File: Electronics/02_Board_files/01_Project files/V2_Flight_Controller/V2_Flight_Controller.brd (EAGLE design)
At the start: 160 x 100 mm, 73 parts

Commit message: 1. Added bmp180.lbr, made changes in 1.25pitch programming connector library 2. Added Datasheets/05_Motor_control/SI2302.pdf 3. Completed top placement for v2 pcb layout
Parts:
- removed 01_BATTERY_PROTECTION_AND_MONITORING:TP_5V: TPB1,27, testpad:B1,27
- added 05_SENSOR:C1, 05_SENSOR:C2: 2.2nF, 50V, ±10%, adafruit:C0603
- added 05_SENSOR:U1: BMP180, bmp180:BMP180
- 07_CONNECTORS:X706: device con-molex:53047-05 -> con-molex_modified:53047-05
- moved 05_SENSOR:C503 276.3 mm to (64.4, 16.0), flipped to the bottom
- moved 05_SENSOR:C502 267.9 mm to (64.2, 12.0), flipped to the bottom
- moved 05_SENSOR:C501 262.5 mm to (66.0, 7.02), flipped to the bottom
- moved 05_SENSOR:R502 258.4 mm to (74.7, 6.02), flipped to the bottom
- moved 06_MOTOR_CONTROL:R604 246.9 mm to (13.0, 3.38), turned to 180 degrees
- moved 06_MOTOR_CONTROL:R603 238.5 mm to (27.0, 5.62)
- moved 06_MOTOR_CONTROL:D603 236.4 mm to (35.5, 8.00)
- moved 05_SENSOR:C504 236.0 mm to (72.6, 20.2), flipped to the bottom
- moved 05_SENSOR:U501 236.0 mm to (72.6, 12.6), flipped to the bottom
- moved 05_SENSOR:R501 233.4 mm to (65.5, 19.0), flipped to the bottom
- moved 06_MOTOR_CONTROL:D604 233.0 mm to (35.5, 32.0), turned to 180 degrees
- moved 06_MOTOR_CONTROL:Q603 232.9 mm to (31.2, 4.50), turned to 270 degrees
- moved 06_MOTOR_CONTROL:R606 232.2 mm to (27.0, 3.38)
- moved 06_MOTOR_CONTROL:R608 230.8 mm to (27.0, 36.6)
- moved 06_MOTOR_CONTROL:Q604 223.7 mm to (31.2, 35.5), turned to 270 degrees
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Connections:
- net +3V3: now also 05_SENSOR:C1.1, 05_SENSOR:C2.1, 05_SENSOR:U1.2, 05_SENSOR:U1.3
- net +5V: no longer 01_BATTERY_PROTECTION_AND_MONITORING:TP_5V.TP
- net 05_SENSOR:SCL: now also 05_SENSOR:U1.5
- net 05_SENSOR:SDA: now also 05_SENSOR:U1.6
- net GND: now also 05_SENSOR:C1.2, 05_SENSOR:C2.2, 05_SENSOR:U1.7
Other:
- board size 160 x 100 mm -> 40 x 40 mm

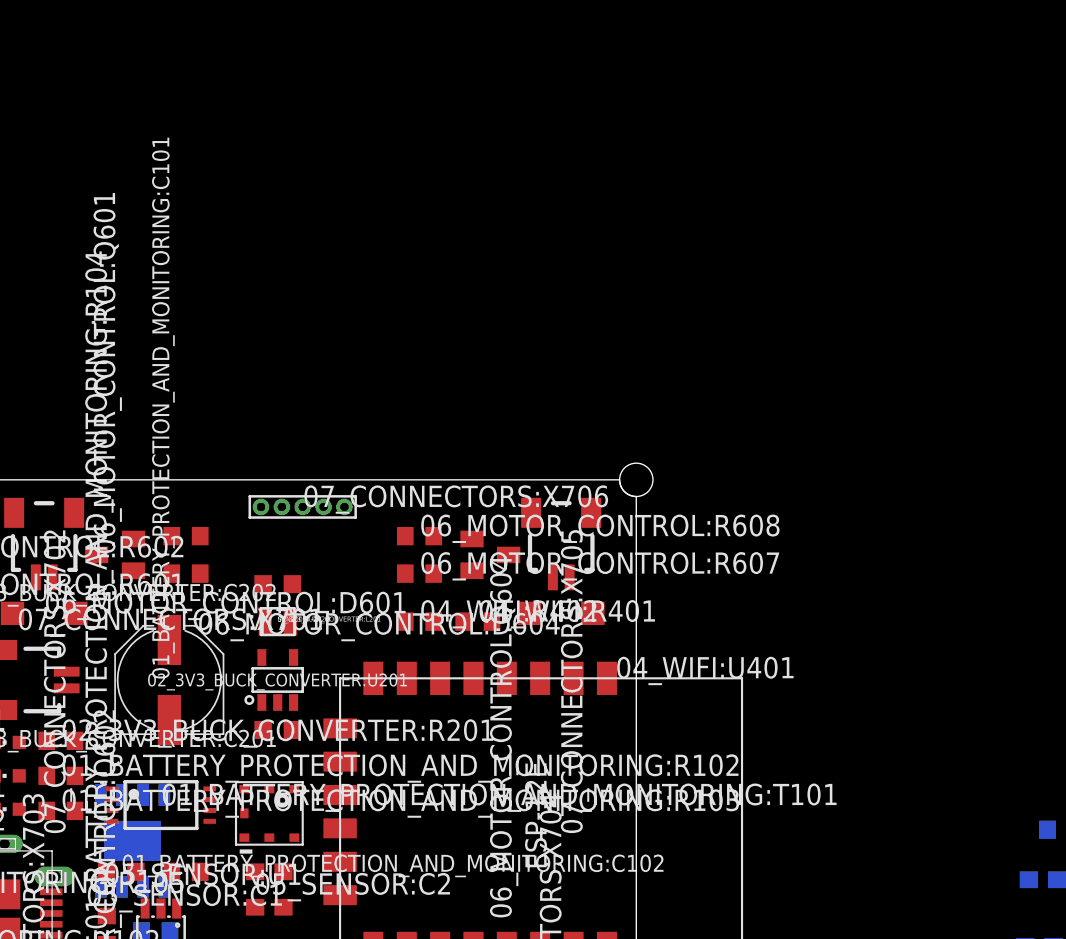
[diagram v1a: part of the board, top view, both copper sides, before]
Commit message: 1. added a bigger input capacitor
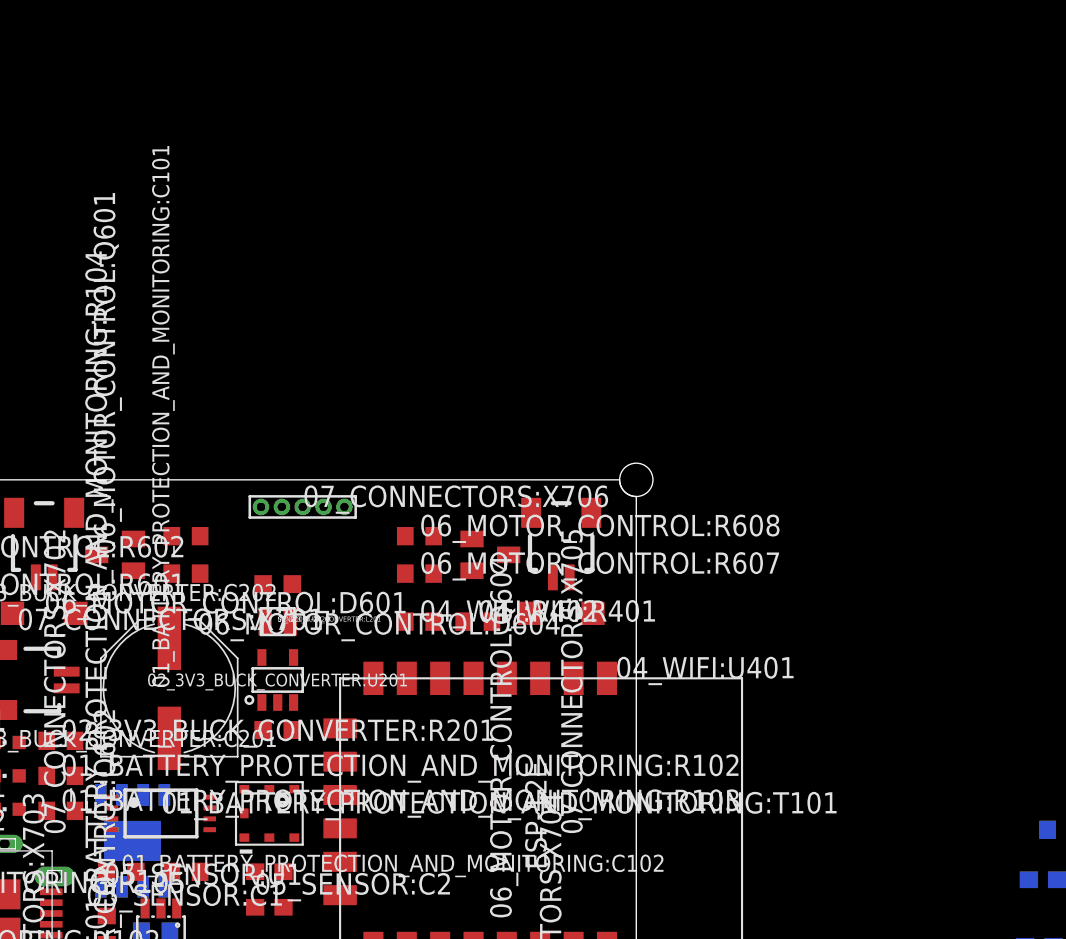
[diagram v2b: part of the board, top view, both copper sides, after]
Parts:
- 01_BATTERY_PROTECTION_AND_MONITORING:C101: device adafruit:PANASONIC_D -> adafruit:PANASONIC_E
- moved 01_BATTERY_PROTECTION_AND_MONITORING:C101 0.50 mm to (12.0, 27.5)
- moved 01_BATTERY_PROTECTION_AND_MONITORING:T101 0.50 mm to (11.5, 20.0)

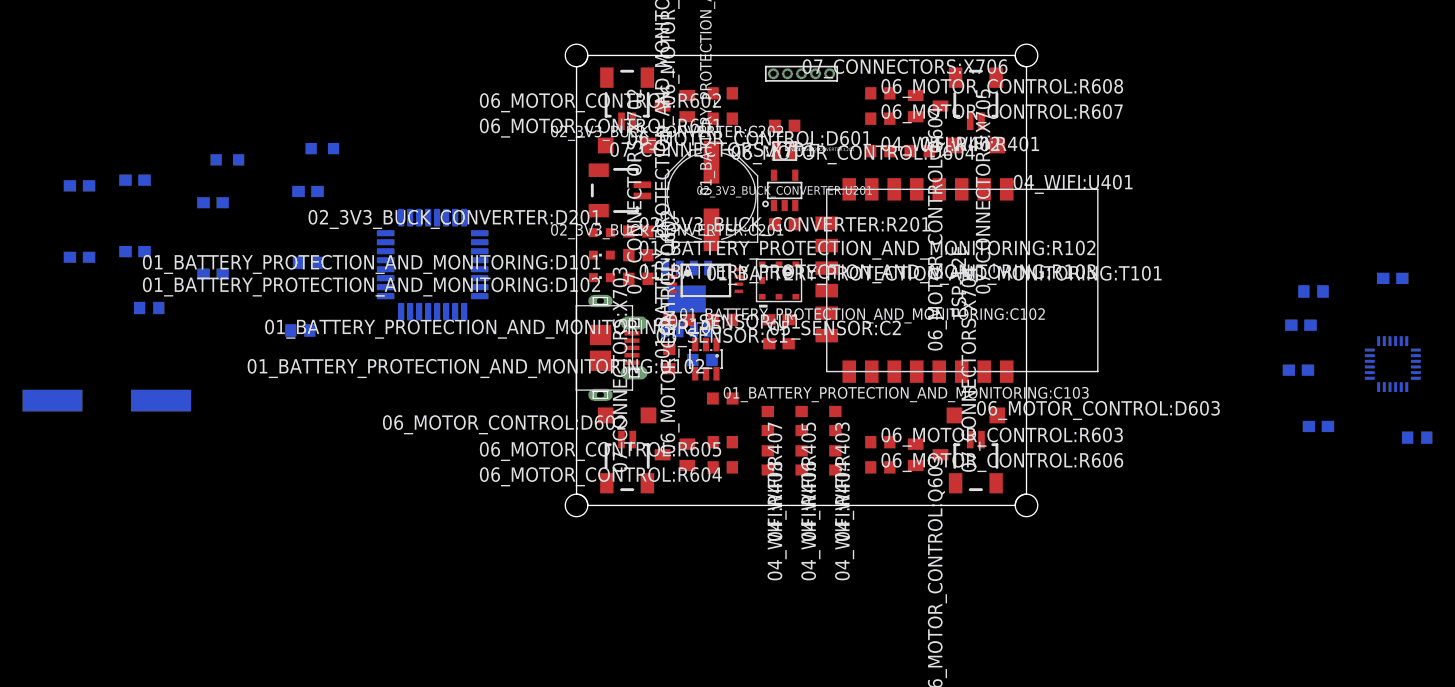
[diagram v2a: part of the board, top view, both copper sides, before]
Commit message: 1. Completed placement and top routing
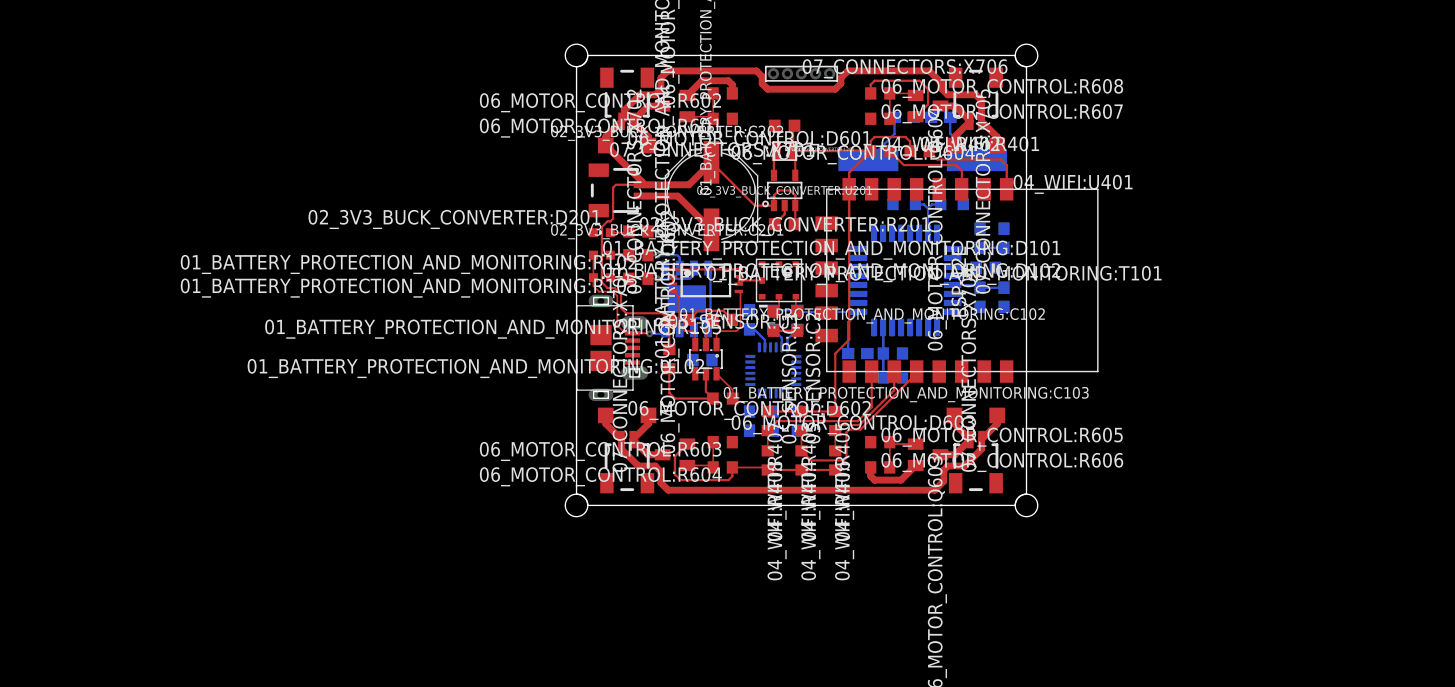
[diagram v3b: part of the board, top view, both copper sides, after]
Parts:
- moved 03_MICROCONTROLLER:C303 80.1 mm to (35.9, 23.8), turned to 90 degrees
- moved 03_MICROCONTROLLER:C307 76.8 mm to (32.4, 34.5)
- moved 03_MICROCONTROLLER:Y301 75.6 mm to (30.8, 30.7), turned to 180 degrees
- moved 03_MICROCONTROLLER:C301 70.4 mm to (38.0, 23.8), turned to 90 degrees
- moved 03_MICROCONTROLLER:C305 68.7 mm to (35.9, 18.5), turned to 270 degrees
- moved 03_MICROCONTROLLER:C306 68.6 mm to (29.1, 34.5), turned to 180 degrees
- moved 03_MICROCONTROLLER:R302 66.4 mm to (28.1, 11.4), turned to 180 degrees
- moved 03_MICROCONTROLLER:C302 64.9 mm to (25.0, 13.5), turned to 180 degrees
- moved 03_MICROCONTROLLER:L303 64.5 mm to (33.4, 26.8), turned to 180 degrees
- moved 03_MICROCONTROLLER:C304 62.6 mm to (38.0, 18.5), turned to 270 degrees
- moved 03_MICROCONTROLLER:R301 61.2 mm to (36.4, 21.1)
- moved 05_SENSOR:C504 58.6 mm to (15.4, 7.50), turned to 270 degrees
- moved 05_SENSOR:R502 56.1 mm to (19.6, 16.5), turned to 270 degrees
- moved 05_SENSOR:U501 55.1 mm to (17.5, 12.0)
- moved 03_MICROCONTROLLER:R303 52.6 mm to (28.1, 13.5)
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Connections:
- removed net 01_BATTERY_PROTECTION_AND_MONITORING:OC: 01_BATTERY_PROTECTION_AND_MONITORING:T101.5, 01_BATTERY_PROTECTION_AND_MONITORING:U102.3
- removed net 01_BATTERY_PROTECTION_AND_MONITORING:OD: 01_BATTERY_PROTECTION_AND_MONITORING:T101.4, 01_BATTERY_PROTECTION_AND_MONITORING:U102.1
- new net 01_BATTERY_PROTECTION_AND_MONITORING:N$1: 01_BATTERY_PROTECTION_AND_MONITORING:T101.4, 01_BATTERY_PROTECTION_AND_MONITORING:U102.3
- new net 01_BATTERY_PROTECTION_AND_MONITORING:N$2: 01_BATTERY_PROTECTION_AND_MONITORING:T101.5, 01_BATTERY_PROTECTION_AND_MONITORING:U102.1
- net BATTERY_+VE: now also 07_CONNECTORS:X703.1, 07_CONNECTORS:X704.2; no longer 07_CONNECTORS:X703.2, 07_CONNECTORS:X704.1
- net M2: now also 07_CONNECTORS:X703.2; no longer 07_CONNECTORS:X703.1
- net M3: now also 07_CONNECTORS:X704.1; no longer 07_CONNECTORS:X704.2
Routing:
- net BATTERY_+VE: track 0.00 -> 136.0 mm
- net +3V3: track 0.00 -> 69.9 mm, vias 0 -> 1
- net GND: track 0.00 -> 52.6 mm
- net +5V: track 0.00 -> 21.7 mm, vias 0 -> 1
- net 04_WIFI:GPIO0: track 0.00 -> 17.3 mm
- net 04_WIFI:GPIO15: track 0.00 -> 15.1 mm
- net BATTERY_-VE: track 0.00 -> 10.8 mm
- net 04_WIFI:GPIO2: track 0.00 -> 10.2 mm
- net 04_WIFI:RST_ESP8266: track 0.00 -> 9.57 mm
- net 04_WIFI:CH_PD: track 0.00 -> 8.78 mm
- net 01_BATTERY_PROTECTION_AND_MONITORING:VCC: track 0.00 -> 8.69 mm
- net 01_BATTERY_PROTECTION_AND_MONITORING:N$2: track 0.00 -> 6.53 mm
- net M2: track 0.00 -> 5.94 mm
- net M1: track 0.00 -> 5.94 mm
- net M4: track 0.00 -> 5.94 mm
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
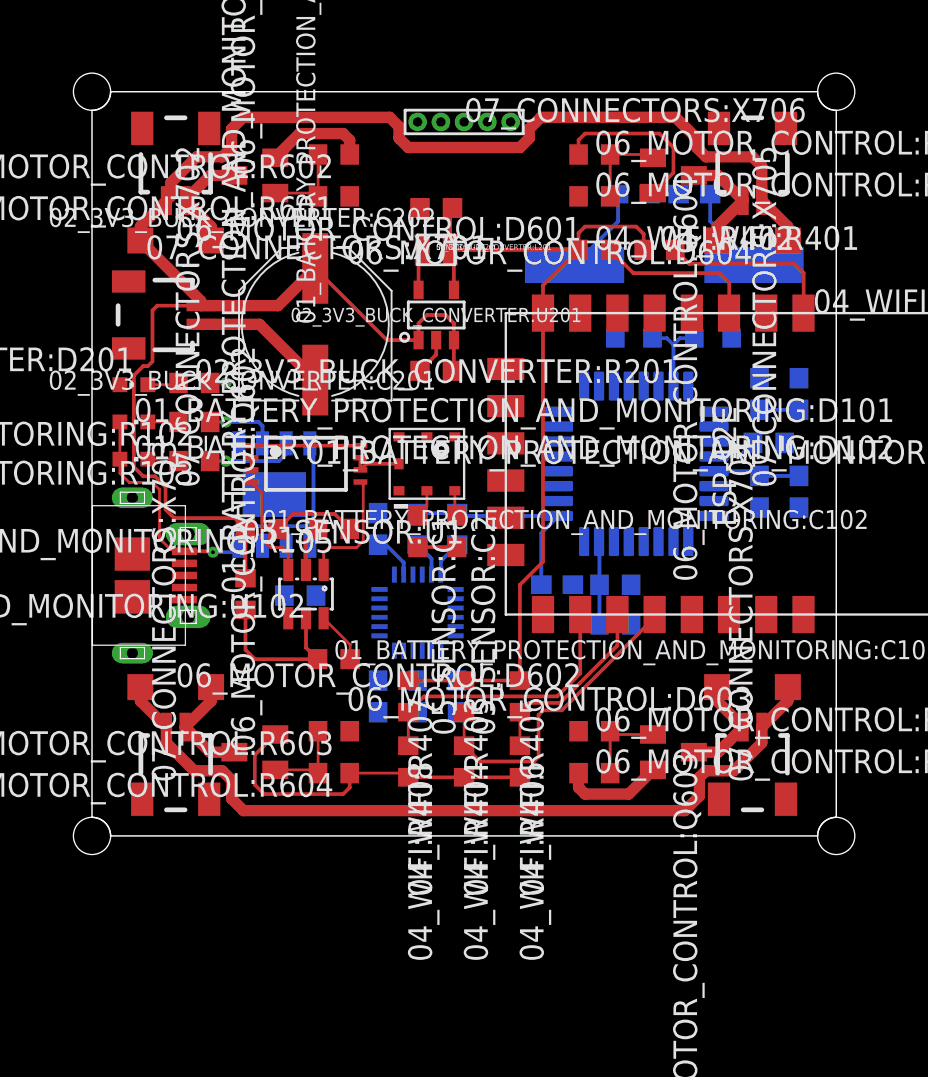
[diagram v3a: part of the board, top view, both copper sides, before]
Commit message: 1. Made changes in pin assignment to help easy routing 2. routed 60% board
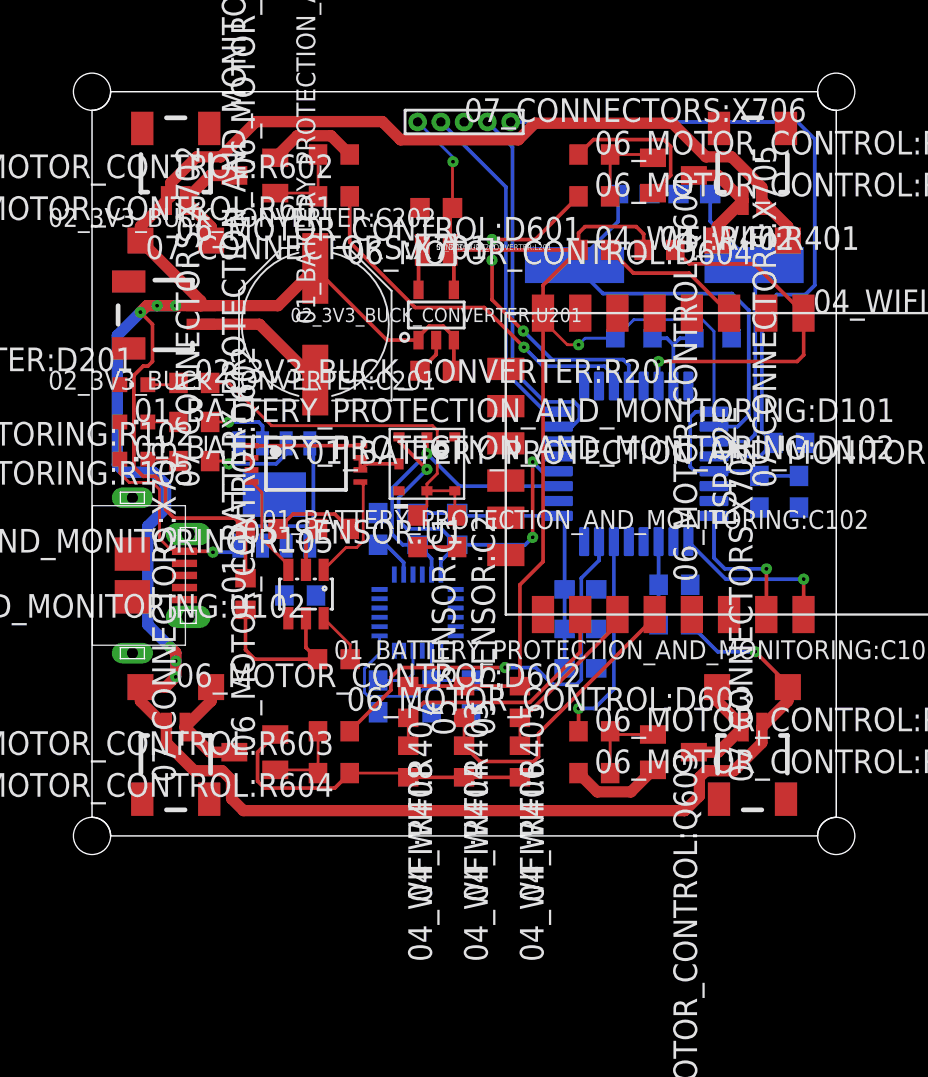
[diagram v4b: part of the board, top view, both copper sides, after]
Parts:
- moved 03_MICROCONTROLLER:C301 18.9 mm to (26.2, 9.00), turned to 180 degrees
- moved 03_MICROCONTROLLER:C303 15.9 mm to (26.2, 11.1), turned to 180 degrees
- moved 03_MICROCONTROLLER:R302 3.18 mm to (31.3, 11.4)
- moved 03_MICROCONTROLLER:R303 3.18 mm to (31.3, 13.5)
- moved 03_MICROCONTROLLER:C302 1.27 mm to (26.2, 13.2)
- moved 03_MICROCONTROLLER:R301 1.10 mm to (37.5, 21.1)
- moved 05_SENSOR:C501 0.75 mm to (18.2, 7.50)
- moved 05_SENSOR:C502 0.75 mm to (20.4, 7.50)
- moved 04_WIFI:R403 0.30 mm to (20.0, 7.20)
- moved 04_WIFI:R405 0.30 mm to (23.0, 7.20)
- moved 04_WIFI:R407 0.30 mm to (17.0, 7.20)
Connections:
- removed net 03_MICROCONTROLLER:IMU_INT: 03_MICROCONTROLLER:U301.10
- removed net 04_WIFI:RST_ESP8266: 04_WIFI:R401.2, 04_WIFI:U401.1
- removed net 05_SENSOR:IMU_INT: 05_SENSOR:U501.12
- removed net 05_SENSOR:SCL: 05_SENSOR:R501.2, 05_SENSOR:U1.5, 05_SENSOR:U501.23
- removed net 05_SENSOR:SDA: 05_SENSOR:R502.2, 05_SENSOR:U1.6, 05_SENSOR:U501.24
- new net IMU_INT: 03_MICROCONTROLLER:U301.10, 05_SENSOR:U501.12
- new net WIFI_RST: 03_MICROCONTROLLER:U301.30, 04_WIFI:R401.2, 04_WIFI:U401.1
- net 03_MICROCONTROLLER:BAT_MON: now also 03_MICROCONTROLLER:U301.11; no longer 03_MICROCONTROLLER:U301.15
- net I2C_SCL: now also 03_MICROCONTROLLER:U301.19, 05_SENSOR:R501.2, 05_SENSOR:U1.5, 05_SENSOR:U501.23; no longer 03_MICROCONTROLLER:U301.29
- net I2C_SDA: now also 03_MICROCONTROLLER:U301.20, 05_SENSOR:R502.2, 05_SENSOR:U1.6, 05_SENSOR:U501.24; no longer 03_MICROCONTROLLER:U301.30
- net M1_PWM: now also 03_MICROCONTROLLER:U301.27; no longer 03_MICROCONTROLLER:U301.19
- net M2_PWM: now also 03_MICROCONTROLLER:U301.15; no longer 03_MICROCONTROLLER:U301.21
- net M3_PWM: now also 03_MICROCONTROLLER:U301.14; no longer 03_MICROCONTROLLER:U301.18
- net M4_PWM: now also 03_MICROCONTROLLER:U301.28; no longer 03_MICROCONTROLLER:U301.20
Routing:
- net +3V3: track 69.9 -> 126.8 mm, vias 1 -> 2
- net NRST: track 2.40 -> 38.9 mm
- net BATTERY_+VE: track 136.0 -> 168.3 mm, vias 0 -> 7
- net M2_PWM: track 0.00 -> 22.6 mm, vias 0 -> 1
- net I2C_SDA: track 0.00 -> 21.3 mm, vias 0 -> 3
- net SWDIO: track 0.00 -> 20.3 mm
- net M1_PWM: track 0.00 -> 20.2 mm, vias 0 -> 1
- net WIFI_RST: track 0.00 -> 19.8 mm, vias 0 -> 1
- net M4_PWM: track 0.00 -> 18.8 mm, vias 0 -> 3
- net SWCLK: track 0.00 -> 18.6 mm
- net 03_MICROCONTROLLER:XTAL_IN: track 4.79 -> 22.9 mm
- net I2C_SCL: track 0.00 -> 17.3 mm, vias 0 -> 1
- net 03_MICROCONTROLLER:XTAL_OUT: track 4.80 -> 16.3 mm
- net M3_PWM: track 0.00 -> 11.5 mm, vias 0 -> 1
- net 04_WIFI:RST_ESP8266: track 9.57 -> 0.00 mm
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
